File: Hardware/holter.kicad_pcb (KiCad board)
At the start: 2 copper layers, 30 x 45 mm, 244 parts, among them CN1 2TAP, IC1 256kx8, Q1 PMF170XP, Q2 PMF170XP, Q3 PMF170XP, Q4 PMF170XP, Q5 PMF170XP, U1 TXB0106, U10 TS5A3159, U11 TS5A3159, U12 ESD_PROTECTOR, U13 ESD_PROTECTOR, U14 ESD_PROTECTOR, U15 ESD_PROTECTOR, U16 ESD_PROTECTOR, U17 ESD_PROTECTOR, U18 ESD_PROTECTOR, U19 ESD_PROTECTOR, U2 TXB0106, U20 ESD_PROTECTOR, U21 ESD_PROTECTOR, U22 ESD_PROTECTOR, U23 ESD_PROTECTOR, U24 TLV61220, U25 TLV61220, U26 TLV61220, U27 LM3671, U28 DS2710, U29 LIS2DH12, U3 TiWi-uB2, U4 STM32F4x1_64, U5 uSD, U6 ADS1298, U7 USBULC6-2M6, U8 USB2641, U9 OPA379

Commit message: Footprints.
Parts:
- added ANT1: 2450AT42A100, Footprints:2450AT42A100, F.Cu at (100.6, 75.6)
- added C62: TPSC337M006R0080, Capacitors_Tantalum_SMD:TantalC_SizeC_EIA-6032_Reflow, F.Cu at (51.9, 62.4)
- added CN2: 2TAP, Resistors_SMD:R_0402, F.Cu at (101.7, 89.5)
- added CONN1: HDMI, Footprints:HDMI10029449, F.Cu at (84.2, 39.3)
- added D1: DB2S20500L, Diodes_SMD:SOD-323, F.Cu at (98.7, 84.1)
- added D3: DB2S20500L, Diodes_SMD:SOD-323, F.Cu at (103.3, 84.2)
- added D4: DB2S20500L, Diodes_SMD:SOD-323, F.Cu at (108.0, 84.5)
- added D7: D_Schottky, Diodes_SMD:SOD-123, F.Cu at (52.1, 58.3)
- added RP1: 51R EXB2HV510JV, Footprints:EXB2HV, F.Cu at (79.5, 86.0)
- added RP2: 100k EXB2HV104JV, Footprints:EXB2HV, F.Cu at (60.6, 47.0)
- added RP3: 51R EXB2HV510JV, Footprints:EXB2HV, F.Cu at (91.7, 89.2)
- added Rsense1: 0.1 1%, Capacitors_SMD:C_0805, F.Cu at (54.8, 54.7)
- added SW1: SW_PUSH, Footprints:MCTA3, F.Cu at (64.5, 76.3)
- CN1: footprint Capacitors_SMD:C_0402 -> Resistors_SMD:R_0402
- IC1, U25, U26: moved to F.Cu
- Q3: value PMF170XP -> NTR4101PT1G; footprint TO_SOT_Packages_SMD:SC-70 -> TO_SOT_Packages_SMD:SOT-23
- U10, U6, U9: moved to B.Cu
- moved FB8 179.4 mm to (81.1, 30.4), turned to 90 degrees
- moved U10 169.4 mm to (79.6, 38.0)
- moved U17 157.0 mm to (82.3, 30.4), turned to 90 degrees
- moved U24 137.2 mm to (85.8, 64.0)
- moved FB1 132.0 mm to (68.9, 28.2), turned to 90 degrees
- moved U9 114.7 mm to (84.1, 38.0), turned to 90 degrees
- moved U28 74.9 mm to (51.0, 54.8)
- moved L4 74.4 mm to (51.8, 48.8), turned to 270 degrees
- moved F1 56.5 mm to (156.8, 65.9)
- moved U27 36.6 mm to (101.6, 51.3)
- moved U5 24.3 mm to (63.5, 57.5)
- moved U1 23.2 mm to (98.8, 58.0), turned to 180 degrees
- moved U26 16.6 mm to (80.7, 63.6)
- moved U2 16.3 mm to (98.8, 64.1)
- moved U6 13.4 mm to (83.8, 47.6)
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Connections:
- C126 pad 1: Net-(C126-Pad1) -> VCC
- C127 pad 1: Net-(C126-Pad1) -> VCC
- L4 pad 2: Net-(C126-Pad1) -> VCC
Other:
- board size 30 x 45 mm -> 33.5 x 45 mm

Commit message: Footprints.
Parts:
- removed LED1, LED2, LED3: LED, LEDs:LED-3MM
- removed R79: R, Resistors_SMD:R_0402
- removed SW1: SW_PUSH, Footprints:MCTA3
- added CN3: 3TAP, Footprints:SOLDERJUMPER3, F.Cu at (90.0, 90.1)
- added D2: D_Schottky, Diodes_SMD:SOD-123, F.Cu at (70.7, 88.0)
- added P1: CONN_01X07, Footprints:MOBO9155, F.Cu at (83.3, 77.1)
- added P2: PROG, Footprints:HEADER127_4, F.Cu at (80.5, 72.0)
- added TH1: NTC, 10k, Resistors_ThroughHole:Resistor_Horizontal_RM10mm, F.Cu at (54.4, 72.8)
- added X1: 32768, Footprints:FC135, F.Cu at (67.8, 73.6)
- added Y1: 24 MHz, Footprints:TSX3225, F.Cu at (63.4, 79.8)
- added Y2: 10 MHz, Footprints:TSX3225, F.Cu at (81.5, 60.0)
- U1, U2: footprint Housings_SSOP:TSSOP-16_4.4x5mm_Pitch0.65mm -> Footprints:RGY16
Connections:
- C126 pad 1: VCC -> Net-(C126-Pad1)
- C127 pad 1: VCC -> Net-(C126-Pad1)
- C14 pad 1: Net-(C14-Pad1) -> GND
- C14 pad 2: GND -> Net-(C14-Pad2)
- C4 pad 1: Net-(C4-Pad1) -> GND
- C4 pad 2: GND -> Net-(C4-Pad2)
- L4 pad 2: VCC -> Net-(C126-Pad1)
- R33 pad 1: Net-(C14-Pad1) -> Net-(C14-Pad2)
- R81 pad 1: Net-(LED2-Pad1) -> R_PWM
- R81 pad 2: R_PWM -> Net-(P1-Pad2)
- R82 pad 1: Net-(LED3-Pad1) -> G_PWM
- R82 pad 2: G_PWM -> Net-(P1-Pad1)
- U4 pad 5: Net-(C3-Pad1) -> Net-(C4-Pad2)
- U4 pad 6: Net-(C4-Pad1) -> Net-(C3-Pad1)
- U8 pad 45: Net-(C14-Pad1) -> Net-(C14-Pad2)

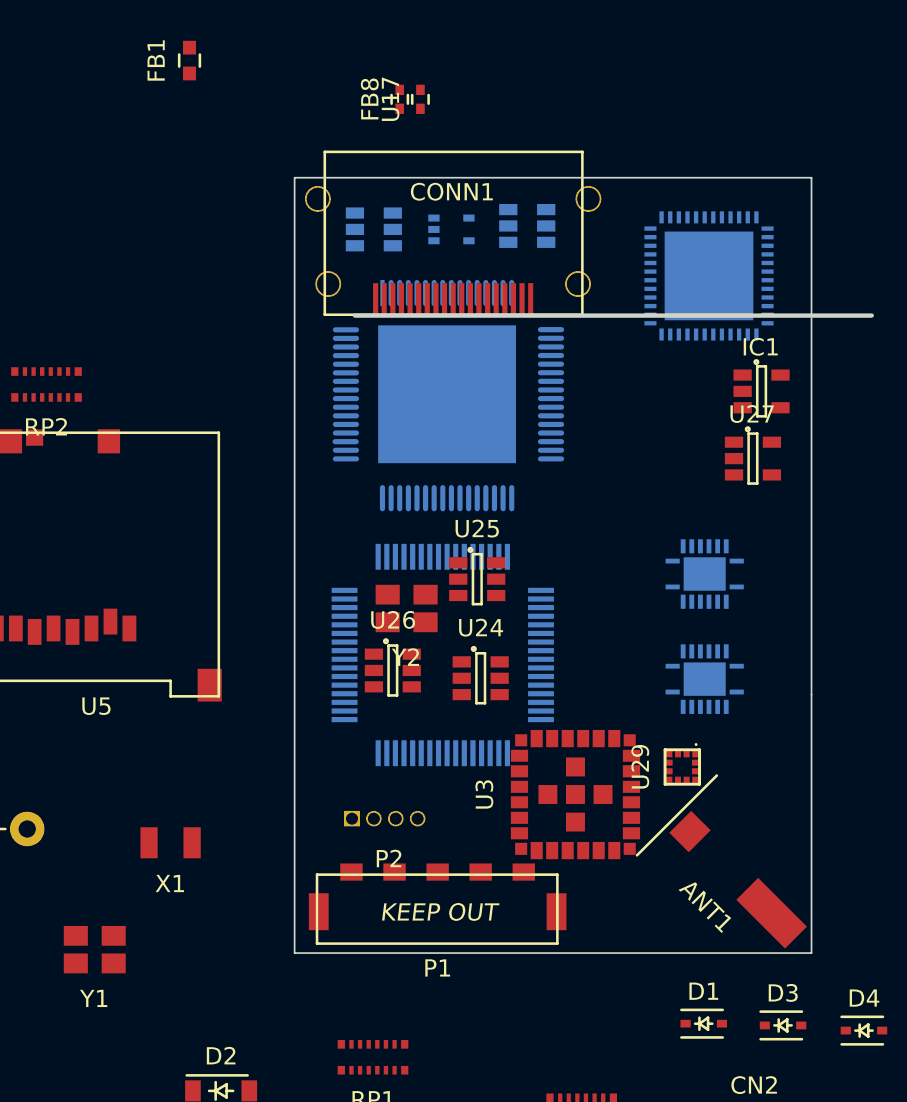
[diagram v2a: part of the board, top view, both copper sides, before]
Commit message: New, surface mounted HDMI connector
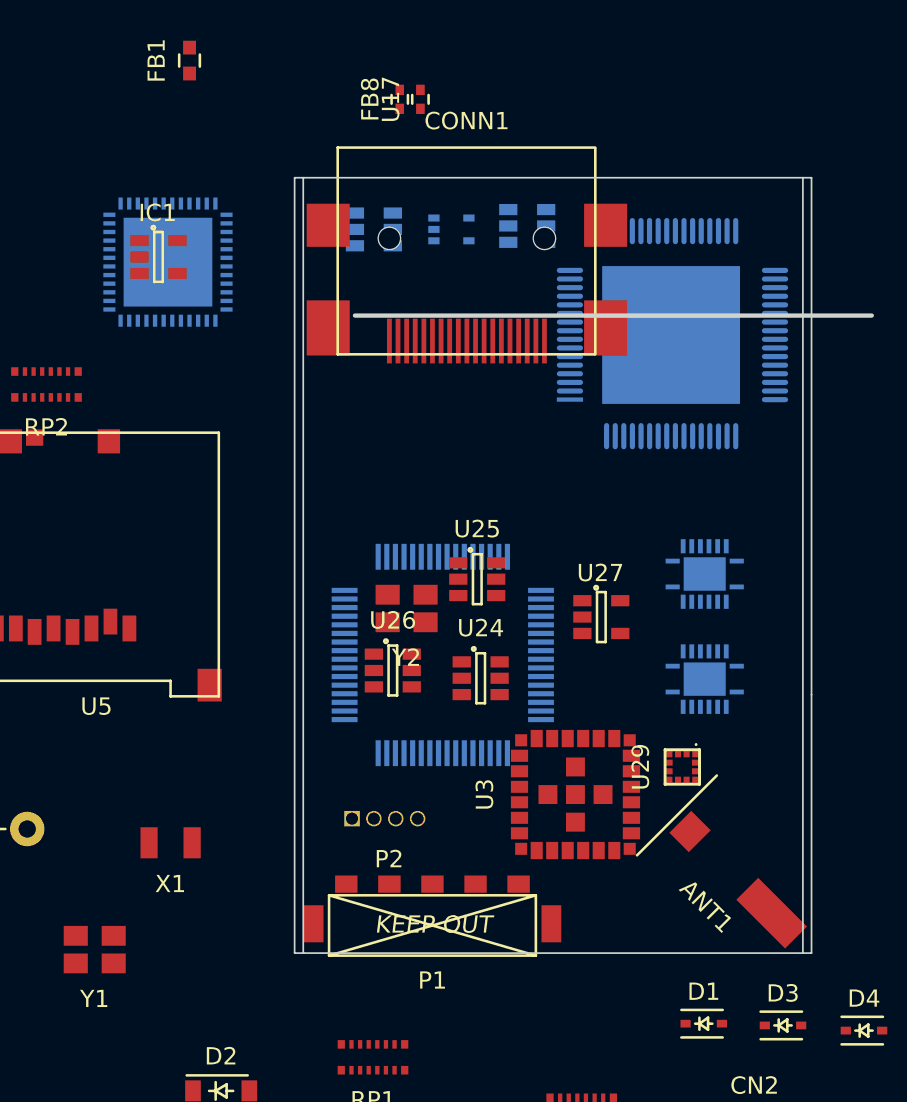
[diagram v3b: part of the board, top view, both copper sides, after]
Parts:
- CONN1: footprint Footprints:HDMI10029449 -> Footprints:MC34931
- moved IC1 35.9 mm to (67.1, 39.6)
- moved U8 31.4 mm to (67.7, 39.9)
- moved U6 13.4 mm to (96.8, 44.1), turned to 90 degrees
- moved U27 12.7 mm to (92.8, 60.5)
- moved CONN1 0.82 mm to (85.0, 39.5)
- moved P1 0.76 mm to (83.0, 77.8)
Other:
- outline, holes or cut-outs redrawn

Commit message: Outline drawings.
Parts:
- U8: moved to F.Cu
- moved IC1 71.5 mm to (138.3, 32.7)
- moved RP2 71.5 mm to (131.8, 40.1)
- moved U28 71.5 mm to (122.2, 47.9)
- moved L4 71.5 mm to (123.0, 41.9)
- moved Rsense1 71.5 mm to (126.0, 47.8)
- moved X1 71.5 mm to (139.0, 66.7)
- moved C62 71.5 mm to (123.1, 55.5)
- moved D7 71.5 mm to (123.3, 51.4)
- moved TH1 71.5 mm to (125.6, 65.9)
- moved U5 71.5 mm to (134.7, 50.6)
- moved Y1 71.5 mm to (134.6, 72.9)
- moved D2 57.9 mm to (128.5, 84.0)
- moved U17 52.1 mm to (134.0, 24.1)
- moved FB1 52.1 mm to (120.6, 21.9)
- moved FB8 52.1 mm to (132.8, 24.1)
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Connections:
- P1 pad 1: Net-(P1-Pad1) -> /BAT+
- P1 pad 2: Net-(P1-Pad2) -> BTN
- P1 pad 4: BTN -> Net-(P1-Pad4)
- P1 pad 5: /BAT+ -> Net-(P1-Pad5)
- R81 pad 2: Net-(P1-Pad2) -> Net-(P1-Pad5)
- R82 pad 2: Net-(P1-Pad1) -> Net-(P1-Pad4)
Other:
- board size 33.5 x 45 mm -> 33.5 x 48 mm

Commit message: Placement...
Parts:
- moved RP2 89.8 mm to (71.1, 106.2)
- moved U5 89.8 mm to (74.0, 116.8)
- moved C62 80.1 mm to (44.8, 72.5)
- moved Q3 51.5 mm to (142.0, 111.9)
- moved D2 43.7 mm to (100.6, 50.4), turned to 180 degrees
- moved Rsense1 36.0 mm to (90.7, 54.4), turned to 180 degrees
- moved U28 31.6 mm to (90.7, 50.1), turned to 270 degrees
- moved D7 27.8 mm to (95.5, 50.4)
- moved L4 24.2 mm to (98.9, 42.4)
- moved U9 3.67 mm to (83.0, 41.5)
- moved U10 3.38 mm to (82.9, 37.2), turned to 180 degrees
- moved U6 3.18 mm to (97.7, 42.3)
- moved U2 1.97 mm to (100.1, 62.6)
- moved U1 1.70 mm to (100.1, 57.0)
- moved U11 1.69 mm to (86.9, 37.2)
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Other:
- net class Default: clearance 0.2 -> 0.15; trace_width 0.25 -> 0.15; via_dia 0.6 -> 0.4; via_drill 0.4 -> 0.15
- rule trace_clearance: 0.2 -> 0.15
- rule trace_min: 0.2 -> 0.15
- rule via_min_drill: 0.3 -> 0.15

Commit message: New HDMI Type-C footprint, BOM
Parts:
- ANT1, IC1, P2, R85, RP3, Rsense1, U24, U25, U26, U27, U29, U3, U5, X1, Y1, Y2: moved to B.Cu
- U1, U2, U4: moved to F.Cu
- moved R85 152.9 mm to (84.3, 65.3), turned to 180 degrees
- moved C21 147.6 mm to (140.9, 24.8)
- moved FB9 143.6 mm to (140.9, 23.6)
- moved F1 79.0 mm to (79.6, 49.0)
- moved Q3 73.5 mm to (114.0, 43.9)
- moved RP3 62.7 mm to (88.3, 57.1), turned to 270 degrees
- moved IC1 61.9 mm to (81.1, 56.5)
- moved Y1 52.1 mm to (86.5, 53.0)
- moved RP1 50.7 mm to (80.0, 69.1)
- moved X1 50.5 mm to (88.7, 62.9), turned to 90 degrees
- moved C62 50.1 mm to (94.8, 70.0)
- moved U5 43.7 mm to (82.8, 73.9), turned to 180 degrees
- moved RP2 39.9 mm to (85.6, 69.1), turned to 180 degrees
- moved U1 26.5 mm to (79.6, 73.7)
- moved P2 21.4 mm to (101.4, 67.6), turned to 180 degrees
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
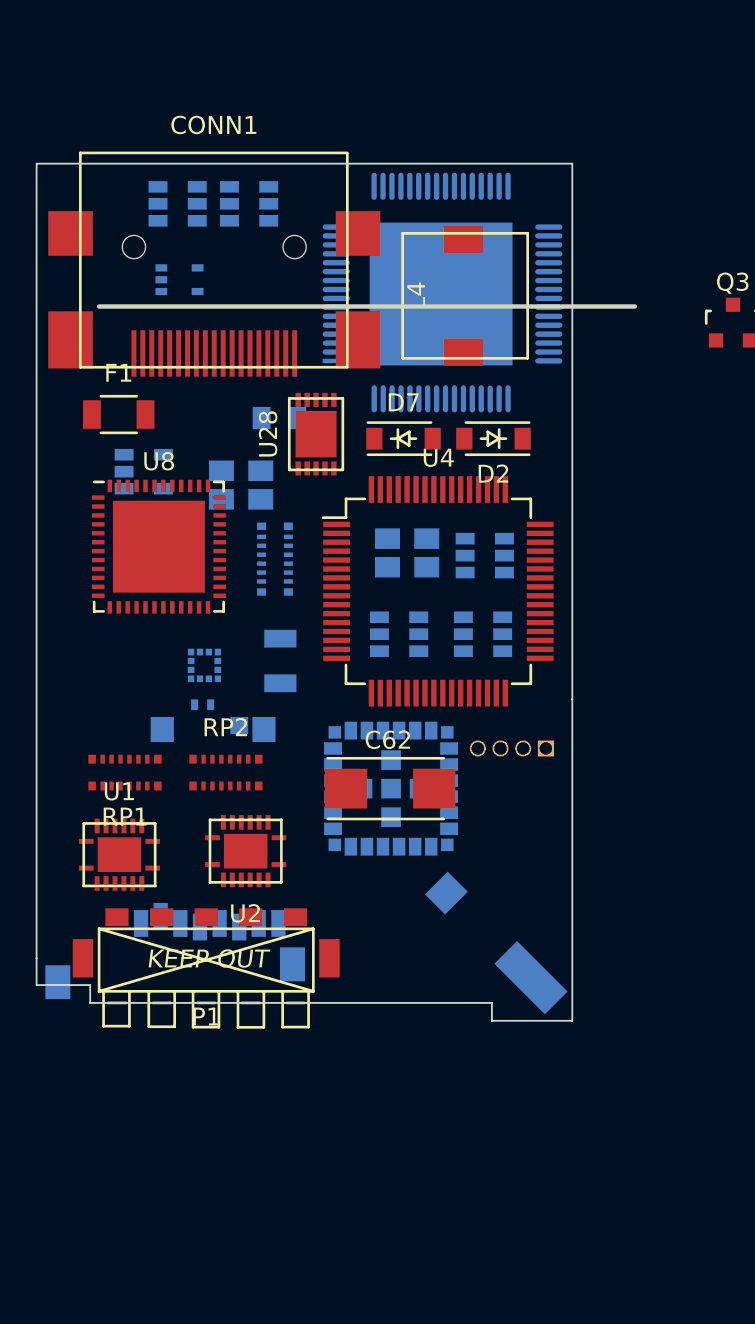
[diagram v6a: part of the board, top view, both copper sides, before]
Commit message: Grounding point, LC filter at 1.8V supply
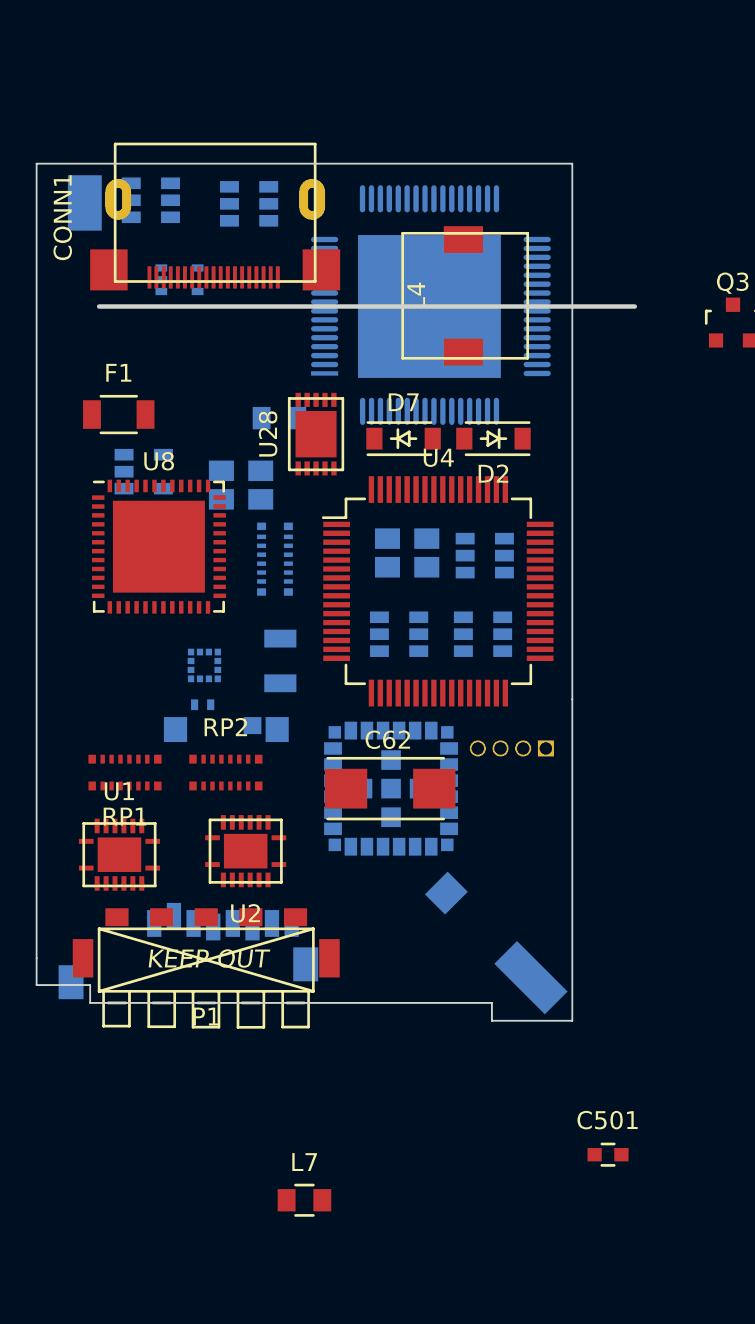
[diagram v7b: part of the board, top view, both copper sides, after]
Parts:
- added C501: 10uF, Capacitors_SMD:C_0603, F.Cu at (107.0, 90.5)
- added L7: 4.7uH, Capacitors_SMD:C_0805, F.Cu at (90.0, 93.1)
- added P4: BAT-, Footprints:S7121-42R, B.Cu at (77.5, 38.0)
- CONN1: footprint Footprints:MC34931 -> Footprints:2013978
- moved CONN1 2.65 mm to (85.0, 38.0), turned to 270 degrees
- moved U10 1.51 mm to (81.4, 37.0)
- moved U6 0.96 mm to (97.0, 43.0)
- moved U5 0.74 mm to (83.5, 73.9)
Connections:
- net B_PWM renamed Net-(U4-Pad61)
- C111 pad 1: VCC -> BAT+
- C113 pad 1: VCC -> BAT+
- C49 pad 1: VCC -> BAT+
- C50 pad 1: VCC -> BAT+
- C54 pad 1: VCC -> BAT+
- C55 pad 1: VCC -> BAT+
- C93 pad 1: +1V8 -> Net-(C93-Pad1)
- C95 pad 1: +1V8 -> Net-(C93-Pad1)
- D2 pad 1: VCC -> BAT+
- L1 pad 1: VCC -> BAT+
- L2 pad 1: VCC -> BAT+
- L3 pad 1: VCC -> BAT+
- P1 pad 1: /BAT+ -> BAT+
- R10 pad 2: VCC -> BAT+
- R68 pad 2: +1V8 -> Net-(C93-Pad1)
- R77 pad 2: VCC -> BAT+
- U24 pad 6: VCC -> BAT+
- U25 pad 3: VCC -> BAT+
- U25 pad 5: +1V8 -> Net-(C93-Pad1)
- U25 pad 6: VCC -> BAT+
- U26 pad 6: VCC -> BAT+

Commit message: PCB mounting
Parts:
- TH1: footprint Resistors_ThroughHole:Resistor_Horizontal_RM10mm -> Capacitors_ThroughHole:C_Disc_D3_P2.5
- U29: moved to F.Cu
- moved U29 4.62 mm to (80.0, 64.5), turned to 270 degrees
- moved L4 2.20 mm to (97.0, 43.5), turned to 0 degrees
- moved P4 2.00 mm to (77.5, 40.0)
- moved R85 1.97 mm to (83.5, 63.5)
- moved U10 1.10 mm to (82.5, 37.0)
- moved U4 0.50 mm to (97.0, 59.0)
- moved U6 0.50 mm to (97.0, 43.5)
